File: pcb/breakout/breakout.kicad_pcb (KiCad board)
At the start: 2 copper layers, 22.9 x 21.6 mm, 6 parts, among them J1 Conn_01x01, J2 Conn_01x01, J3 Conn_01x01, J4 Conn_01x01, SW1 SW_DIP_x01

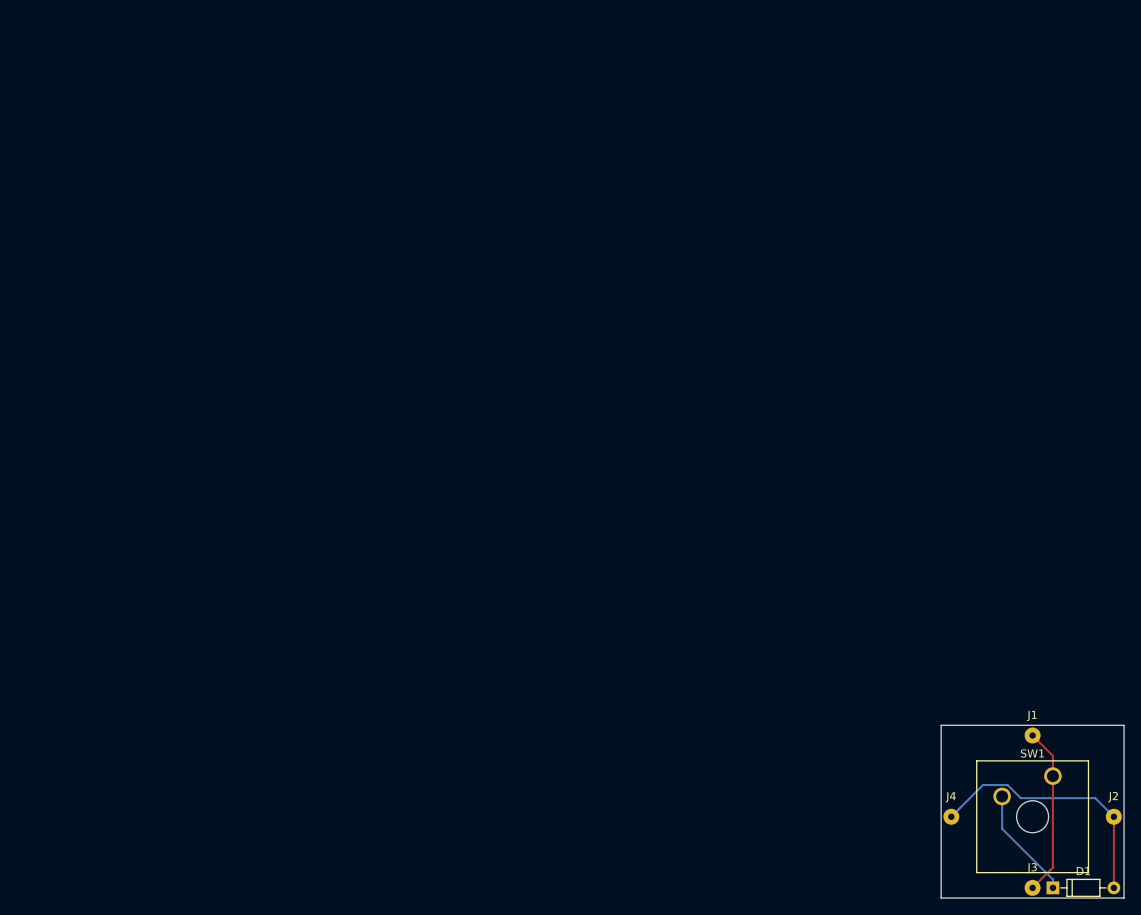
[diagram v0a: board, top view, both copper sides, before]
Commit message: reduction breakout
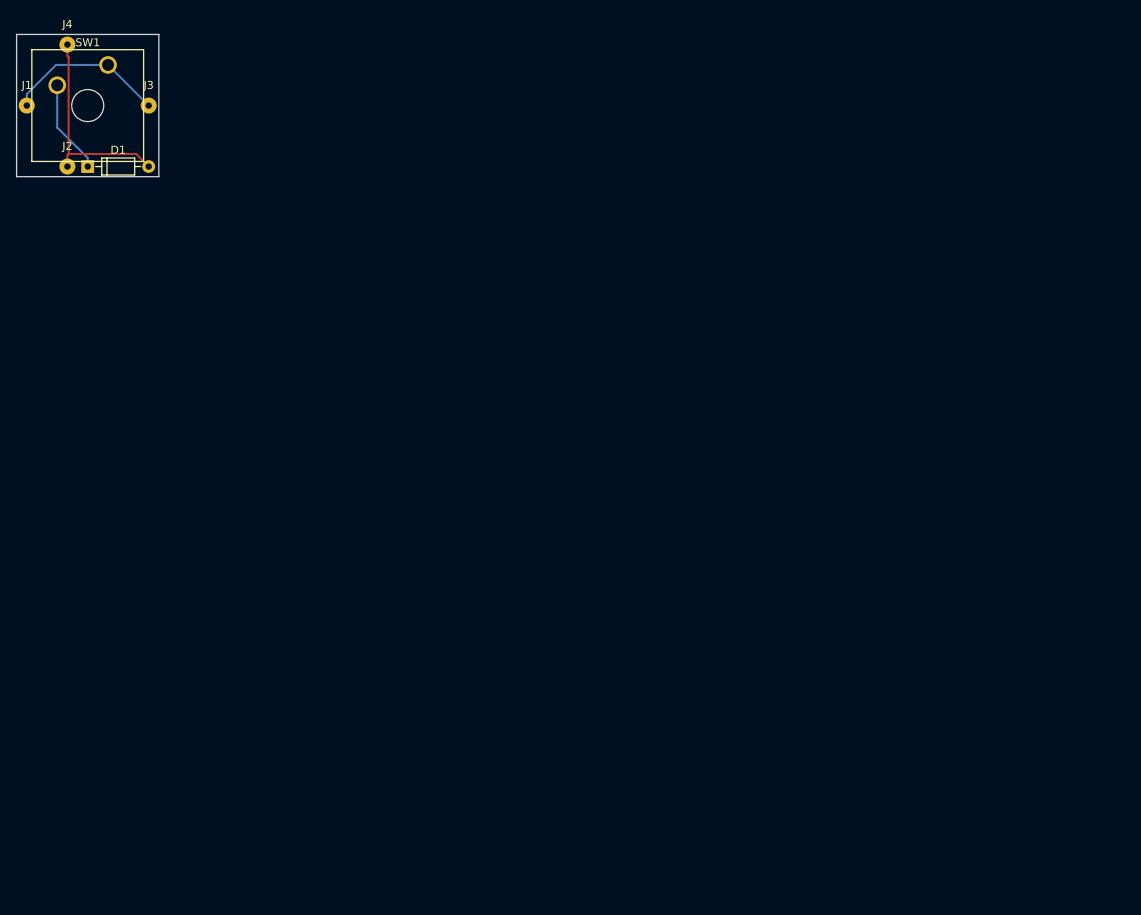
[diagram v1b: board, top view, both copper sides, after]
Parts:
- moved J2 154.0 mm to (7.62, 17.8)
- moved D1 150.6 mm to (10.2, 17.8)
- moved J1 148.4 mm to (2.54, 10.2)
- moved SW1 147.8 mm to (12.7, 5.08)
- moved J3 147.5 mm to (17.8, 10.2)
- moved J4 146.7 mm to (7.62, 2.54)
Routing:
- net Net-(D1-Pad2): track 32.5 -> 26.0 mm
- net Net-(D1-Pad1): track 14.1 -> 11.7 mm
- net Net-(J1-Pad1): track 21.2 -> 20.3 mm
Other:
- board size 22.9 x 21.6 mm -> 17.8 x 17.8 mm
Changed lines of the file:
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@@
     (links 5)
     (no_connects 0)
-    (area 0 0 0 0)
+    (area 1.194999 1.194999 19.125001 19.125001)
     (thickness 1.6)
     (drawings 4)
@@
   )
   (module Diodes_THT:D_DO-35_SOD27_P7.62mm_Horizontal (layer F.Cu)
-    (at 130.81 107.95)
+    (at 10.16 17.78)
     (descr "D, DO-35_SOD27 series, Axial, Horizontal, pin pitch=7.62mm, , length*diameter=4*2mm^2, , http://www.diodes.com/_files/packages/DO-35.pdf")
     (tags "D DO-35_SOD27 series Axial Horizontal pin pitch 7.62mm  length 4mm diameter 2mm")
@@
   )
   (module Wire_Pads:SolderWirePad_single_0-8mmDrill (layer F.Cu)
-    (at 128.27 88.9)
+    (at 2.54 10.16)
     (fp_text reference J1 (at 0 -2.54) (layer F.SilkS)
       (effects (font (size 1 1) (thickness 0.15)))
@@
   )
   (module Wire_Pads:SolderWirePad_single_0-8mmDrill (layer F.Cu)
-    (at 138.43 99.06)
+    (at 7.62 17.78)
     (fp_text reference J2 (at 0 -2.54) (layer F.SilkS)
       (effects (font (size 1 1) (thickness 0.15)))
@@
   )
   (module Buttons_Switches_Keyboard:SW_Cherry_MX1A_1.00u_Plate (layer F.Cu)
-    (at 130.81 93.98)
+    (at 12.7 5.08)
     (descr "Cherry MX keyswitch, MX1A, 1u, plate mount, http://cherryamericas.com/wp-content/uploads/2014/12/mx_cat.pdf")
     (tags "cherry mx keyswitch MX1A 1u plate")
@@
   )
   (module Wire_Pads:SolderWirePad_single_0-8mmDrill (layer F.Cu)
-    (at 128.27 107.95)
+    (at 17.78 10.16)
     (fp_text reference J3 (at 0 -2.54) (layer F.SilkS)
       (effects (font (size 1 1) (thickness 0.15)))
@@
   )
   (module Wire_Pads:SolderWirePad_single_0-8mmDrill (layer F.Cu)
-    (at 118.11 99.06)
+    (at 7.62 2.54)
     (fp_text reference J4 (at 0 -2.54) (layer F.SilkS)
       (effects (font (size 1 1) (thickness 0.15)))
@@
       (net 2 "Net-(D1-Pad2)"))
   )
-  (gr_line (start 116.84 109.22) (end 116.84 87.63) (layer Edge.Cuts) (width 0.15))
-  (gr_line (start 139.7 109.22) (end 116.84 109.22) (layer Edge.Cuts) (width 0.15))
-  (gr_line (start 139.7 87.63) (end 139.7 109.22) (layer Edge.Cuts) (width 0.15))
-  (gr_line (start 116.84 87.63) (end 139.7 87.63) (layer Edge.Cuts) (width 0.15))
-  (segment (start 130.81 107.95) (end 130.81 106.9) (width 0.25) (layer B.Cu) (net 1))
-  (segment (start 130.81 106.9) (end 124.46 100.55) (width 0.25) (layer B.Cu) (net 1))
-  (segment (start 124.46 100.55) (end 124.46 98.075634) (width 0.25) (layer B.Cu) (net 1))
-  (segment (start 124.46 98.075634) (end 124.46 96.52) (width 0.25) (layer B.Cu) (net 1))
-  (segment (start 138.43 99.06) (end 136.104999 96.734999) (width 0.25) (layer B.Cu) (net 2))
-  (segment (start 136.104999 96.734999) (end 126.784001 96.734999) (width 0.25) (layer B.Cu) (net 2))
-  (segment (start 126.784001 96.734999) (end 125.144001 95.094999) (width 0.25) (layer B.Cu) (net 2))
-  (segment (start 125.144001 95.094999) (end 122.075001 95.094999) (width 0.25) (layer B.Cu) (net 2))
-  (segment (start 122.075001 95.094999) (end 119.109489 98.060511) (width 0.25) (layer B.Cu) (net 2))
-  (segment (start 119.109489 98.060511) (end 118.11 99.06) (width 0.25) (layer B.Cu) (net 2))
-  (segment (start 138.43 99.06) (end 138.43 107.95) (width 0.25) (layer F.Cu) (net 2))
-  (segment (start 130.81 93.98) (end 130.81 91.44) (width 0.25) (layer F.Cu) (net 3))
-  (segment (start 130.81 91.44) (end 128.27 88.9) (width 0.25) (layer F.Cu) (net 3))
-  (segment (start 128.27 107.95) (end 130.81 105.41) (width 0.25) (layer F.Cu) (net 3))
-  (segment (start 130.81 105.41) (end 130.81 93.98) (width 0.25) (layer F.Cu) (net 3))
+  (gr_line (start 1.27 19.05) (end 1.27 1.27) (layer Edge.Cuts) (width 0.15))
+  (gr_line (start 19.05 19.05) (end 1.27 19.05) (layer Edge.Cuts) (width 0.15))
+  (gr_line (start 19.05 1.27) (end 19.05 19.05) (layer Edge.Cuts) (width 0.15))
+  (gr_line (start 1.27 1.27) (end 19.05 1.27) (layer Edge.Cuts) (width 0.15))
+  (segment (start 10.16 17.78) (end 10.16 16.73) (width 0.25) (layer B.Cu) (net 1))
+  (segment (start 10.16 16.73) (end 6.35 12.92) (width 0.25) (layer B.Cu) (net 1))
+  (segment (start 6.35 12.92) (end 6.35 9.175634) (width 0.25) (layer B.Cu) (net 1))
+  (segment (start 6.35 9.175634) (end 6.35 7.62) (width 0.25) (layer B.Cu) (net 1))
+  (segment (start 17.78 17.78) (end 16.211507 16.211507) (width 0.25) (layer F.Cu) (net 2))
+  (segment (start 16.211507 16.211507) (end 7.775001 16.211507) (width 0.25) (layer F.Cu) (net 2))
+  (segment (start 7.62 2.54) (end 7.62 3.953492) (width 0.25) (layer F.Cu) (net 2))
+  (segment (start 7.62 3.953492) (end 7.775001 4.108493) (width 0.25) (layer F.Cu) (net 2))
+  (segment (start 7.775001 4.108493) (end 7.775001 16.211507) (width 0.25) (layer F.Cu) (net 2))
+  (segment (start 7.775001 16.211507) (end 7.62 16.366508) (width 0.25) (layer F.Cu) (net 2))
+  (segment (start 7.62 16.366508) (end 7.62 17.78) (width 0.25) (layer F.Cu) (net 2))
+  (segment (start 12.7 5.08) (end 6.206508 5.08) (width 0.25) (layer B.Cu) (net 3))
+  (segment (start 6.206508 5.08) (end 2.54 8.746508) (width 0.25) (layer B.Cu) (net 3))
+  (segment (start 2.54 8.746508) (end 2.54 10.16) (width 0.25) (layer B.Cu) (net 3))
+  (segment (start 12.7 5.08) (end 17.78 10.16) (width 0.25) (layer B.Cu) (net 3))
 )
